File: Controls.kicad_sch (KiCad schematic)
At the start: 0 parts

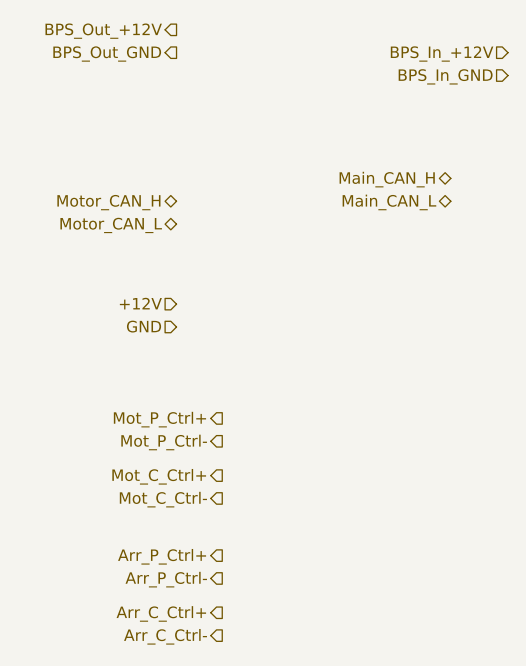
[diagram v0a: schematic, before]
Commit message: Updated Contactors, and fixed a few minor LV things
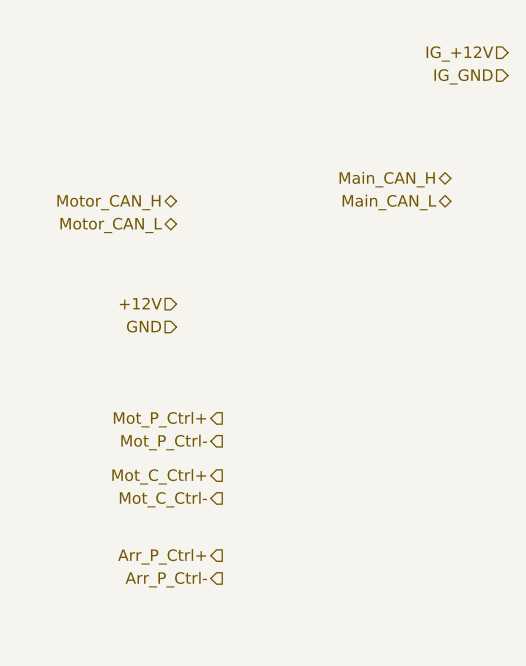
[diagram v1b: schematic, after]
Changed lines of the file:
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@@
     (effects (font (size 1.27 1.27)) (justify right))
   )
-  (hierarchical_label "BPS_Out_GND" (shape output) (at 38.1 78.74 180) (fields_autoplaced)
-    (effects (font (size 1.27 1.27)) (justify right))
-  )
-  (hierarchical_label "BPS_In_+12V" (shape input) (at 74.93 78.74 180) (fields_autoplaced)
+  (hierarchical_label "IG_+12V" (shape input) (at 74.93 78.74 180) (fields_autoplaced)
     (effects (font (size 1.27 1.27)) (justify right))
   )
@@
     (effects (font (size 1.27 1.27)) (justify right))
   )
-  (hierarchical_label "Arr_C_Ctrl+" (shape output) (at 43.18 140.97 180) (fields_autoplaced)
-    (effects (font (size 1.27 1.27)) (justify right))
-  )
   (hierarchical_label "Mot_C_Ctrl-" (shape output) (at 43.18 128.27 180) (fields_autoplaced)
     (effects (font (size 1.27 1.27)) (justify right))
@@
     (effects (font (size 1.27 1.27)) (justify right))
   )
-  (hierarchical_label "Arr_C_Ctrl-" (shape output) (at 43.18 143.51 180) (fields_autoplaced)
-    (effects (font (size 1.27 1.27)) (justify right))
-  )
-  (hierarchical_label "BPS_Out_+12V" (shape output) (at 38.1 76.2 180) (fields_autoplaced)
-    (effects (font (size 1.27 1.27)) (justify right))
-  )
   (hierarchical_label "Mot_P_Ctrl+" (shape output) (at 43.18 119.38 180) (fields_autoplaced)
     (effects (font (size 1.27 1.27)) (justify right))
   )
-  (hierarchical_label "BPS_In_GND" (shape input) (at 74.93 81.28 180) (fields_autoplaced)
+  (hierarchical_label "IG_GND" (shape input) (at 74.93 81.28 180) (fields_autoplaced)
     (effects (font (size 1.27 1.27)) (justify right))
   )
